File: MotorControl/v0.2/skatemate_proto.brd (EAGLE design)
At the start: 126.5 x 87.3 mm, 104 parts, among them IC1 REG1117, Q1 IRF740, Q2 IRF740, Q3 IRF740, Q4 IRF740, Q5 IRF740, Q6 IRF740, U1 DRV8301DCAR

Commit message: layouting on v0.2
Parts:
- removed Q1, Q2, Q3, Q4, Q5, Q6: IRF740, transistor-power:TO220BV
- removed SV1, SV2: (no value), skatemate:MA12-1
- added C39: 2u2, skatemate:C1206
- TP1: value TPSMD_M_1006 -> SUPPLY
- TP2: value TPSMD_M_1006 -> GND
- TP3: value TPSMD_M_1006 -> PH_A
- TP4: value TPSMD_M_1006 -> PH_B
- TP5: value TPSMD_M_1006 -> PH_C
- moved TP1 30.3 mm to (78.5, 7.62), turned to 90 degrees
- moved C6 28.0 mm to (83.8, 52.8), turned to 180 degrees
- moved C7 25.8 mm to (83.6, 30.0), turned to 180 degrees
- moved U$4 24.3 mm to (91.2, 71.4)
- moved U$6 24.3 mm to (91.2, 46.0)
- moved U$8 24.3 mm to (91.2, 20.6)
- moved U$5 17.1 mm to (98.8, 58.7), flipped to the bottom, turned to 90 degrees
- moved U$7 17.1 mm to (98.8, 33.3), flipped to the bottom, turned to 90 degrees
- moved U$9 17.1 mm to (98.8, 7.87), flipped to the bottom, turned to 90 degrees
- moved R6 15.8 mm to (87.6, 3.56), flipped to the bottom, turned to 180 degrees
- moved R4 15.7 mm to (92.7, 27.4), flipped to the bottom, turned to 180 degrees
- moved R2 15.7 mm to (92.7, 52.8), flipped to the bottom, turned to 180 degrees
- moved TP4 15.0 mm to (104.1, 46.0), flipped to the bottom, turned to 270 degrees
- moved TP5 14.8 mm to (104.1, 20.6), flipped to the bottom, turned to 270 degrees
- moved TP3 14.5 mm to (104.1, 71.4), flipped to the bottom, turned to 270 degrees
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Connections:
- net +5V: no longer SV1.3
- net ASENSE: no longer SV2.9
- net BSENSE: no longer SV2.10
- net CSENSE: no longer SV2.11
- net DRV_DCCAL: no longer SV1.11
- net DRV_EN_GATE: no longer SV1.12
- net DRV_NCS: no longer SV1.7
- net DRV_NFAULT: no longer SV1.6
- net DRV_NOCTW: no longer SV1.5
- net DRV_PWRGD: no longer SV1.4
- net DRV_SCK: no longer SV1.10
- net DRV_SDI: no longer SV1.8
- net DRV_SDO: no longer SV1.9
- net DRV_SOA: no longer SV2.7
- net DRV_SOB: no longer SV2.8
- net GND: now also C39.2; no longer Q6.S, SV1.2
- net INH_A: no longer SV2.1
- net INH_B: no longer SV2.3
- net INH_C: no longer SV2.5
- net INL_A: no longer SV2.2
- net INL_B: no longer SV2.4
- net INL_C: no longer SV2.6
- net N$10: no longer Q2.G
- net N$11: no longer Q3.G
- net N$12: no longer Q6.G
- net N$7: no longer Q1.G
- net N$8: no longer Q4.G
- net N$9: no longer Q5.G
- net PH_A: no longer Q1.S, Q4.D
- net PH_B: no longer Q2.S, Q5.D
- net PH_C: no longer Q3.S, Q6.D
- net SN_A: no longer Q4.S
- net SN_B: no longer Q5.S
- net SSENSE: no longer SV2.12
- net SUPPLY: now also C39.1; no longer Q1.D, Q2.D, Q3.D
- net VCC: no longer SV1.1
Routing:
- net VCC: track 317.3 -> 125.5 mm, vias 16 -> 7
- net SUPPLY: track 162.9 -> 18.9 mm, vias 3 -> 1
- net ASENSE: track 157.2 -> 37.8 mm, vias 2 -> 0
- net BSENSE: track 139.6 -> 41.6 mm, vias 2 -> 0
- net PH_B: track 93.3 -> 13.4 mm, vias 3 -> 1
- net PH_C: track 113.0 -> 35.8 mm, vias 3 -> 1
- net GND: track 267.1 -> 193.5 mm, vias 36 -> 30
- net CSENSE: track 122.8 -> 50.4 mm, vias 2 -> 0
- net PH_A: track 107.5 -> 42.0 mm, vias 3 -> 1
- net SN_A: track 95.8 -> 34.1 mm
- net SSENSE: track 115.1 -> 54.5 mm
- net SN_B: track 65.9 -> 14.2 mm, vias 2 -> 0
- net DRV_SCK: track 78.8 -> 45.0 mm
- net DRV_SDO: track 75.4 -> 42.8 mm
- net DRV_SDI: track 71.9 -> 39.9 mm
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- added copper zone on layer 16, net SN_A
- added copper zone on layer 16, net SN_B
- removed copper zone on layer 1, net +5V
- removed copper zone on layer 1, net SN_A
- removed copper zone on layer 1, net SN_B
- removed copper zone on layer 1, net SUPPLY
- removed copper zone on layer 1, net VCC
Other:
- board size 126.5 x 87.3 mm -> 167.4 x 87.6 mm
- board text added: "FHNW 2017 - p4 team 2"
- board text added: "skatemate-motorcontrol v0.2"
- board text removed: "FHNW 2017 - p2 team 2"
- board text removed: "skatemate-motorcontrol v0.1"

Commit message: Öpdeit, Meh gmoolet
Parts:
- moved U$3 45.6 mm to (62.5, 23.1), turned to 90 degrees
- moved R20 5.59 mm to (83.8, 9.65)
- moved C22 5.36 mm to (60.7, 64.8)
- moved D4 4.83 mm to (66.5, 63.8)
- moved R14 4.07 mm to (58.4, 64.0)
- moved R15 4.07 mm to (58.4, 68.1)
- moved L1 3.64 mm to (68.1, 70.6)
- moved C21 2.84 mm to (72.4, 33.3)
- moved D3 2.62 mm to (69.6, 5.33)
- moved D1 2.62 mm to (69.6, 12.4)
- moved D2 2.62 mm to (69.6, 8.89)
- moved D5 2.40 mm to (69.6, 1.78)
- moved R3 2.09 mm to (98.8, 51.3)
- moved C2 1.70 mm to (75.2, 37.6)
- moved C16 1.55 mm to (60.5, 37.8)
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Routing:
- net BSENSE: track 41.6 -> 139.3 mm, vias 0 -> 6
- net ASENSE: track 37.8 -> 134.8 mm, vias 0 -> 2
- net DRV_NCS: track 58.5 -> 17.1 mm, vias 1 -> 0
- net USB_D+: track 38.7 -> 0.00 mm, vias 4 -> 0
- net USB_D-: track 33.8 -> 1.25 mm, vias 4 -> 1
- net GND: track 193.5 -> 162.5 mm, vias 30 -> 29
- net VCC: track 125.5 -> 96.6 mm, vias 7 -> 1
- net GL_B: track 9.40 -> 35.6 mm, vias 0 -> 1
- net SN_A: track 34.1 -> 59.2 mm, vias 2 -> 4
- net DRV_SCK: track 45.0 -> 21.1 mm
- net DRV_SDO: track 42.8 -> 19.7 mm
- net DRV_SOB: track 48.1 -> 25.7 mm
- net DRV_SDI: track 39.9 -> 17.7 mm
- net DRV_SOA: track 47.1 -> 25.6 mm
- net CSENSE: track 50.4 -> 70.9 mm, vias 0 -> 4
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
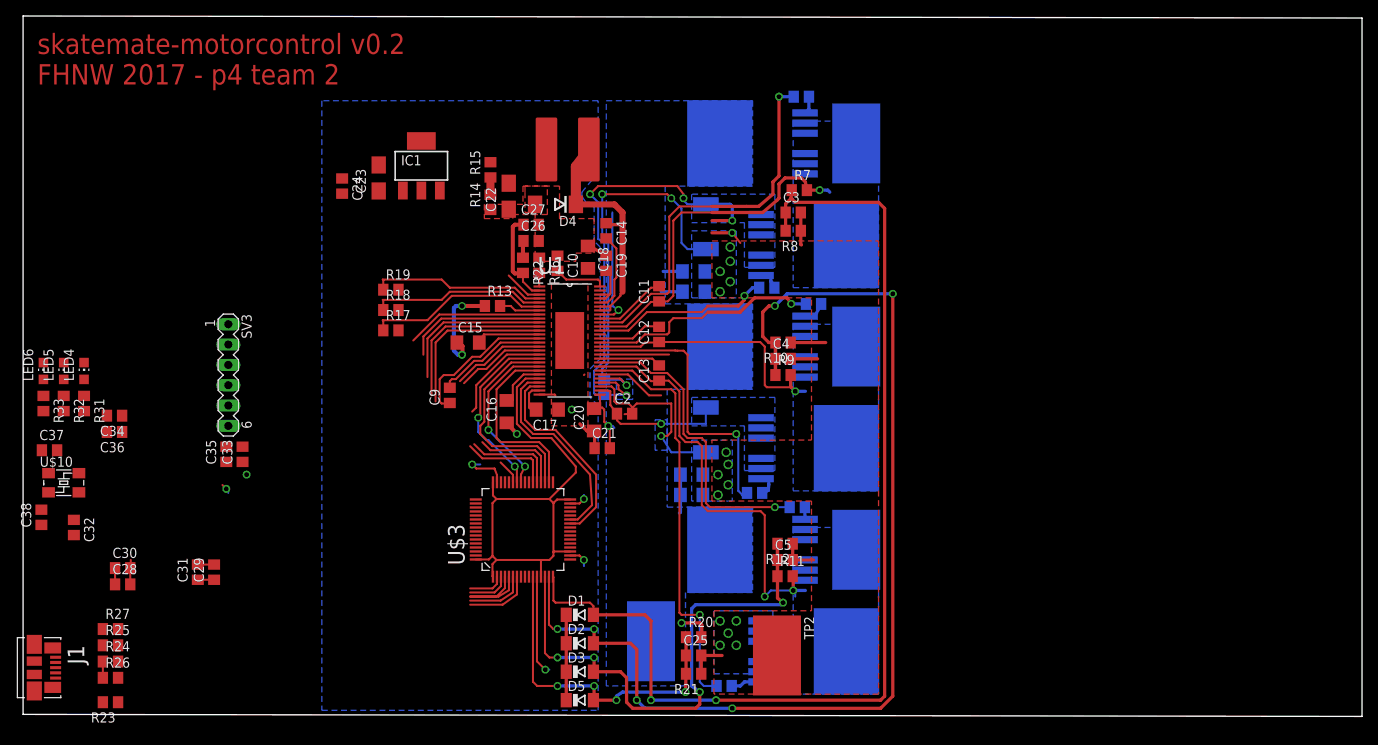
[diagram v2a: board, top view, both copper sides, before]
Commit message: no wiiter gmacht....
Kondensatoren noch unter IC pflanzen, Stecker Layouten, eine VCC Leitung
mit 100uF versehen.
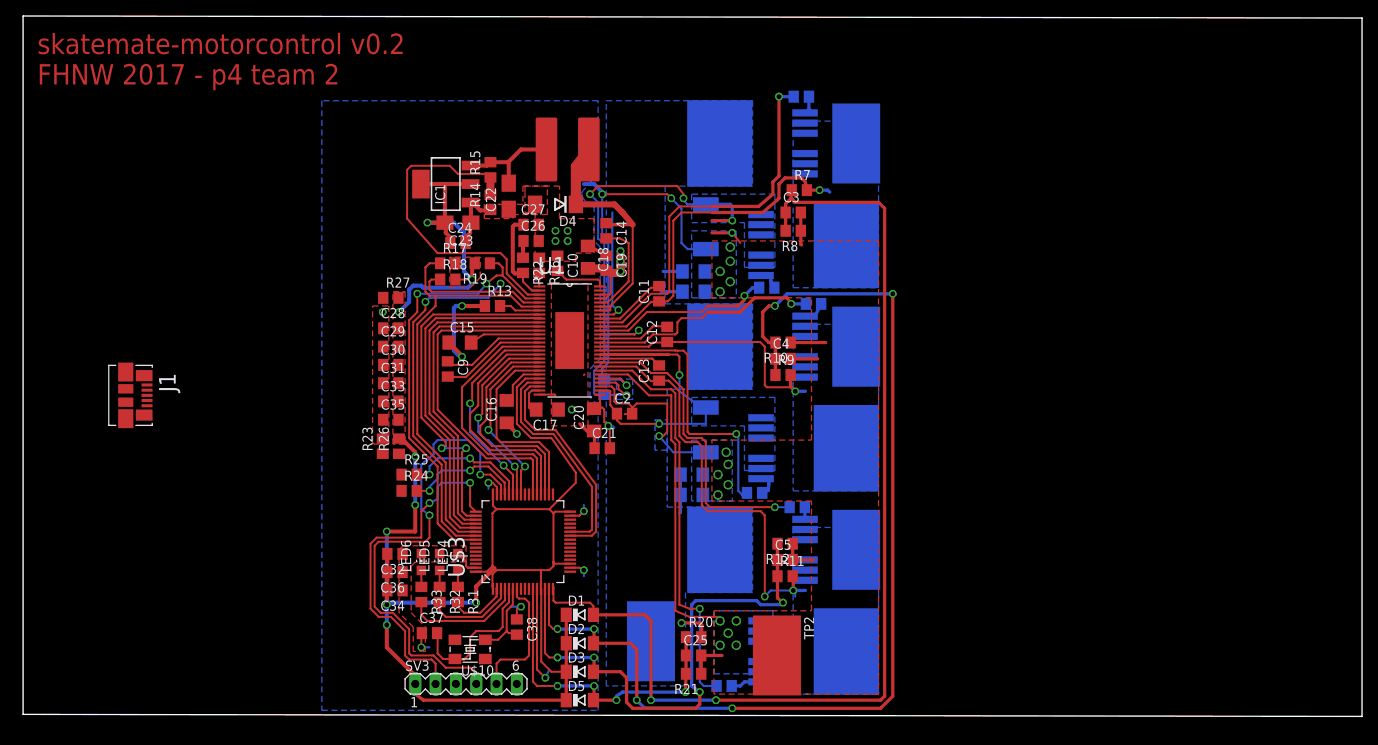
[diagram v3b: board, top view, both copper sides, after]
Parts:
- moved C38 61.0 mm to (61.7, 10.9), turned to 270 degrees
- moved U$10 54.9 mm to (55.9, 8.13), turned to 180 degrees
- moved R27 54.2 mm to (46.0, 52.1)
- moved LED6 52.9 mm to (49.8, 19.1)
- moved R33 52.9 mm to (49.8, 15.0)
- moved C37 52.7 mm to (50.8, 10.2)
- moved LED5 52.7 mm to (52.1, 19.1)
- moved R32 52.7 mm to (52.1, 15.0)
- moved LED4 52.5 mm to (54.4, 19.1)
- moved R31 52.5 mm to (54.4, 15.0)
- moved SV3 48.7 mm to (55.4, 3.81), turned to 0 degrees
- moved R23 46.7 mm to (45.0, 33.5), turned to 90 degrees
- moved C28 46.4 mm to (46.0, 48.3)
- moved R26 46.3 mm to (47.0, 33.5), turned to 90 degrees
- moved R24 43.0 mm to (48.3, 27.9)
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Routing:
- net VCC: track 96.6 -> 232.2 mm, vias 1 -> 10
- net SWDIO: track 0.00 -> 60.8 mm, vias 0 -> 2
- net GND: track 162.5 -> 210.9 mm, vias 29 -> 35
- net SWCLK: track 0.00 -> 46.2 mm, vias 0 -> 2
- net DRV_NOCTW: track 21.9 -> 62.8 mm, vias 0 -> 2
- net DRV_PWRGD: track 21.9 -> 56.4 mm, vias 0 -> 2
- net N$4: track 6.99 -> 41.3 mm
- net DRV_NFAULT: track 22.7 -> 54.9 mm
- net DRV_NCS: track 17.1 -> 45.3 mm, vias 0 -> 2
- net DRV_SDI: track 17.7 -> 43.7 mm
- net DRV_SDO: track 19.7 -> 41.7 mm
- net DRV_SCK: track 21.1 -> 40.0 mm
- net SN_B: track 27.2 -> 44.1 mm, vias 1 -> 2
- net USB_D+: track 0.00 -> 15.2 mm, vias 0 -> 2
- net USB_D-: track 1.25 -> 15.8 mm, vias 1 -> 2
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- added copper zone on layer 1, net VCC

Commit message: layout before review
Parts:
- moved J1 30.9 mm to (44.2, 28.4)
- moved C28 28.5 mm to (62.2, 24.9), flipped to the bottom, turned to 90 degrees
- moved C29 28.1 mm to (64.5, 24.9), flipped to the bottom, turned to 90 degrees
- moved C31 27.8 mm to (65.5, 21.6), flipped to the bottom, turned to 180 degrees
- moved C35 23.2 mm to (59.9, 18.3), flipped to the bottom, turned to 270 degrees
- moved C30 22.1 mm to (57.7, 24.9), flipped to the bottom, turned to 90 degrees
- moved R27 20.1 mm to (47.0, 32.0)
- moved C33 19.9 mm to (59.9, 24.9), flipped to the bottom, turned to 90 degrees
- moved C36 18.0 mm to (64.5, 18.3), flipped to the bottom, turned to 270 degrees
- moved C32 15.8 mm to (62.2, 18.3), flipped to the bottom, turned to 270 degrees
- moved C34 11.5 mm to (57.7, 18.3), flipped to the bottom, turned to 270 degrees
- moved R23 10.4 mm to (44.5, 23.1), turned to 180 degrees
- moved R26 7.64 mm to (47.5, 25.9), turned to 0 degrees
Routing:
- net VCC: track 232.2 -> 318.7 mm
- net SN_A: track 68.8 -> 84.9 mm, vias 5 -> 6
- net GND: track 210.9 -> 218.7 mm, vias 35 -> 42
- net N$22: track 0.00 -> 5.75 mm
- net N$23: track 0.00 -> 5.67 mm
- net SWDIO: track 60.8 -> 55.4 mm
- net SWCLK: track 46.2 -> 40.9 mm
- net N$25: track 0.00 -> 3.51 mm
- net N$24: track 0.00 -> 3.48 mm
- net SN_B: track 44.1 -> 45.6 mm
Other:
- board size 167.4 x 87.6 mm -> 72.1 x 81.7 mm

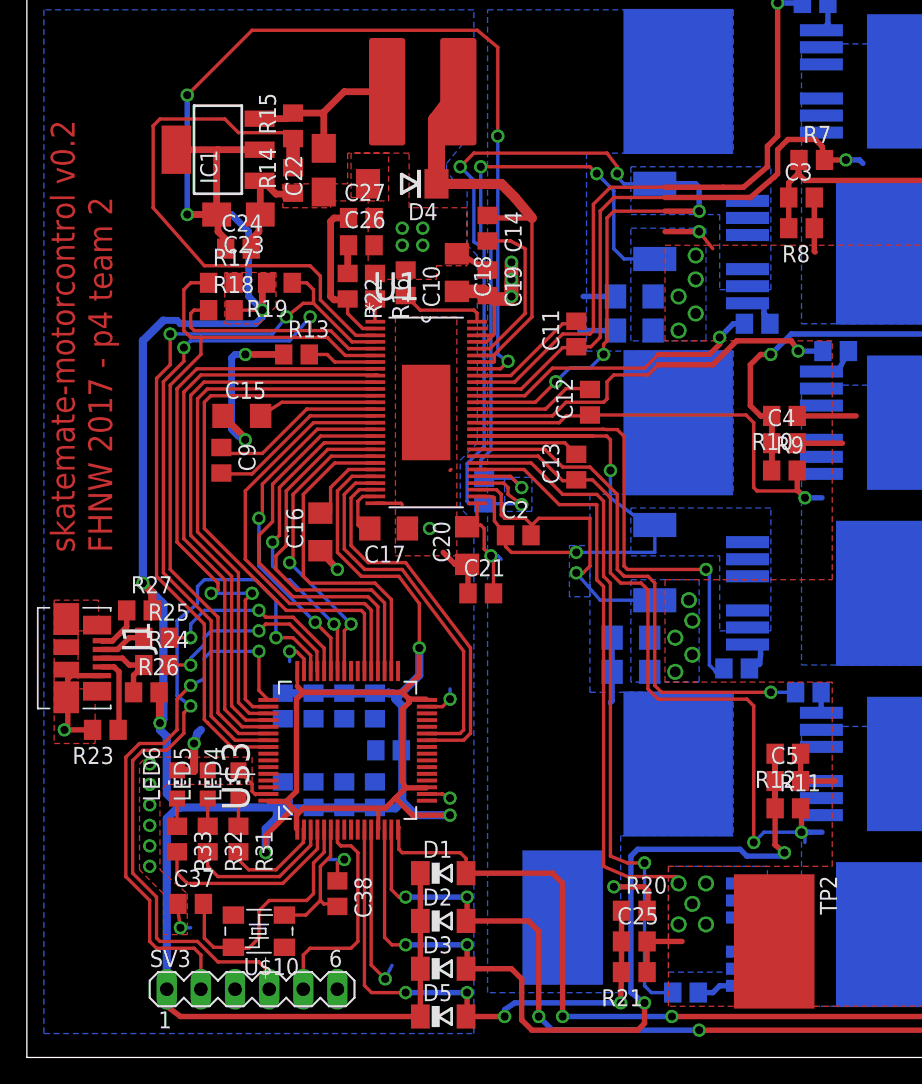
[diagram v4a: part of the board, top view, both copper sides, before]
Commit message: Parts renumber and BOM ULP
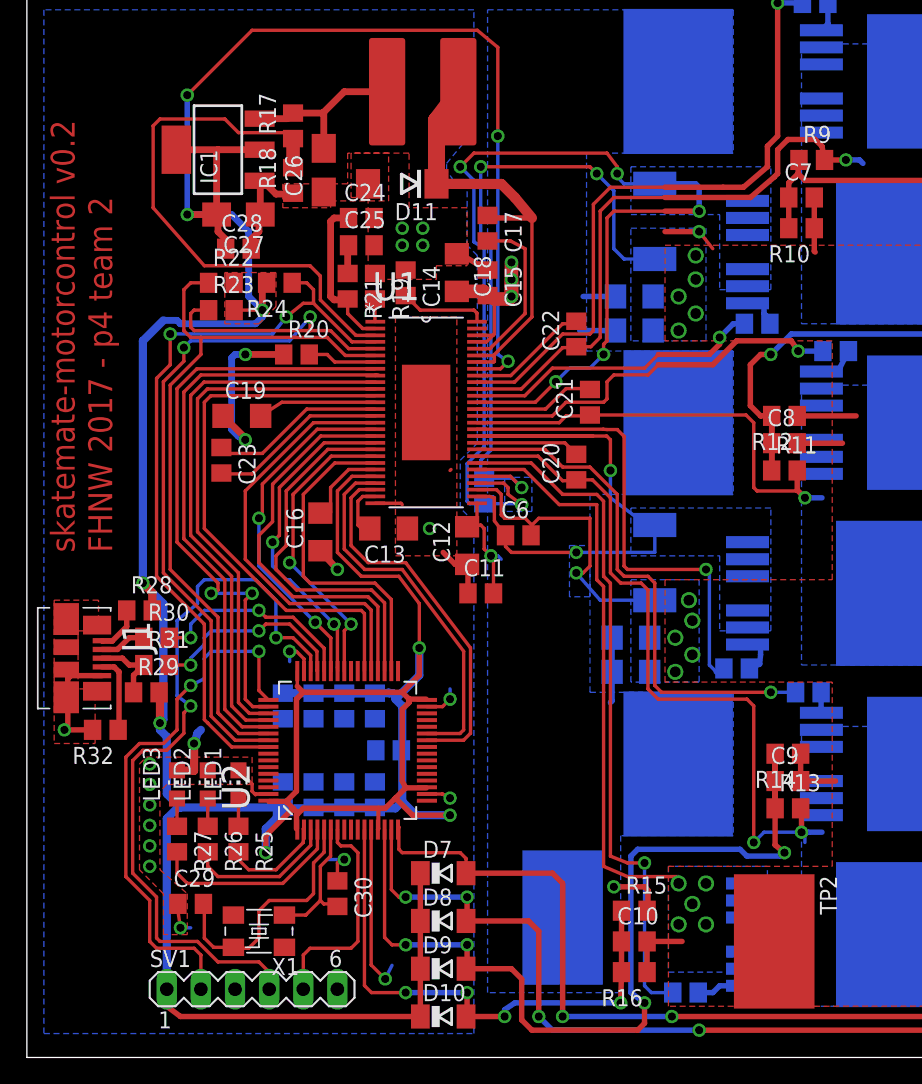
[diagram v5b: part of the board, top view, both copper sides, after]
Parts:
- removed R33: 3k3, skatemate:R0805
- removed U$1, U$2: R_EU, skatemate:R2512
- removed U$4, U$5, U$6, U$7, U$8: IRFS7534, skatemate:D2PAK-7
- added D10, D7, D8, D9: BAS85, skatemate:SOD80C
- added D11: SSA210, skatemate:DO-214AA
- added R28: 0 *, skatemate:R0805
- added R29: 1k5, skatemate:R0805
- added R30: 22, skatemate:R0805
- C10: value 10nF -> 47p
- C11, C21: value 0.1u -> 100n
- C12: value 0.1u -> 4u7; device skatemate:C0805 -> skatemate:C1206
- C13: value 0.1u -> 1u; device skatemate:C0805 -> skatemate:C1206
- C14: value 0.1u -> 10n
- C15: value 2.2u -> 100n; device skatemate:C1206 -> skatemate:C0805
- C17: value 1u -> 100n; device skatemate:C1206 -> skatemate:C0805
- C18: value 4.7u -> 4u7
- C19: value 0.1u -> 2u2; device skatemate:C0805 -> skatemate:C1206
- C2: value (none) -> 2u2; device skatemate:C0805 -> skatemate:C1206
- C20: value 4.7u -> 100n; device skatemate:C1206 -> skatemate:C0805
- C22: value 100u -> 100n; device skatemate:B/3528-21W -> skatemate:C0805
- C23: value 100u -> (none); device skatemate:B/3528-21W -> skatemate:C0805
- C24: value 0.1u -> 150p
- C25: value 47p -> 6n8
- C26: value 6n8 -> 100u; device skatemate:C0805 -> skatemate:B/3528-21W
- C27: value 150p -> 100u; device skatemate:C0805 -> skatemate:B/3528-21W
- C28, C33, C34: value 2u2 -> 100n
- C29: value 2u2 -> 22p
- C3, C4, C5: value 47p -> 2u2; device skatemate:C0805 -> skatemate:C1206
- C30: value 100n -> 22p
- C31, C32, C36: value 100n -> 2u2
- C37: value 22p -> 2u2
- C38: value 22p -> 100n
- C39: value 2u2 -> 100n; device skatemate:C1206 -> skatemate:C0805
- C6: value 2u2 -> (none); device skatemate:C1206 -> skatemate:C0805
- C7, C8: value 2u2 -> 47p; device skatemate:C1206 -> skatemate:C0805
- C9: value (none) -> 47p
- D1, D2, D3, D5: value BAS85 -> IRFS7534; device skatemate:SOD80C -> skatemate:D2PAK-7
- D4: value SSA210 -> IRFS7534; device skatemate:DO-214AA -> skatemate:D2PAK-7
- R13: value 10k -> 39k
- R14: value 3k3 -> 2k2
- R15: value 18k -> 39k
- R16: value 220k -> 2k2
- R18: value 18k -> 3k3
- R19: value 18k -> 220k
- R20: value 39k -> 10k
- R21: value 2k2 -> 16k
- R22: value 16k -> 18k
- R23: value 100k -> 18k
- R24: value 22 -> 18k
- R25: value 22 -> 3k3
- R26: value 1k5 -> 3k3
- R27: value 0 * -> 3k3
- R3, R6: value (none) -> R_EU; device skatemate:R0805 -> skatemate:R2512
- R31: value 3k3 -> 22
- R32: value 3k3 -> 100k
- R7: value 39k -> (none)
- R8: value 2k2 -> (none)
- moved R15 63.7 mm to (83.8, 9.65), turned to 0 degrees
- moved D1 62.8 mm to (91.2, 71.4), flipped to the bottom, turned to 270 degrees
- moved D2 57.7 mm to (98.8, 58.7), flipped to the bottom, turned to 90 degrees
- moved R8 57.5 mm to (87.6, 3.56), flipped to the bottom
- moved R14 56.4 mm to (95.2, 21.3), turned to 180 degrees
- moved C25 55.7 mm to (63.5, 59.2)
- moved R21 55.3 mm to (62.5, 56.1), turned to 270 degrees
- moved R16 54.6 mm to (83.8, 5.08), turned to 180 degrees
- moved C10 51.9 mm to (83.8, 7.37), turned to 0 degrees
- moved R13 49.8 mm to (95.2, 17.3)
- moved C9 48.5 mm to (95.2, 19.3), turned to 0 degrees
- moved R20 48.4 mm to (58.7, 51.1)
- moved D3 46.0 mm to (91.2, 46.0), flipped to the bottom, turned to 270 degrees
- moved D4 44.4 mm to (98.8, 33.3), flipped to the bottom, turned to 90 degrees
- moved C39 41.8 mm to (64.5, 18.3), turned to 270 degrees
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- renumbered LED4 to LED1, LED5 to LED2, LED6 to LED3, SV3 to SV1, U$10 to X1, U$3 to U2, U$9 to D6
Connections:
- net +5V: now also C26.+, R17.2; no longer C22.+, R15.2
- net ASENSE: now also C7.1, D7.A, R10.2, R9.1; no longer C3.1, D1.A, R7.1, R8.2
- net BSENSE: now also C8.1, D8.A, R11.1, R12.2; no longer C4.1, D2.A, R10.2, R9.1
- net BST_BK: now also C17.1, D11.C; no longer C14.1, D4.C
- net CSENSE: now also C9.1, D9.A, R13.1, R14.2; no longer C5.1, D3.A, R11.1, R12.2
- net DRV_NFAULT: now also R22.1; no longer R17.1
- net DRV_NOCTW: now also R23.1; no longer R18.1
- net DRV_PWRGD: now also R24.1; no longer R19.1
- net GH_B: now also R4.1; no longer R3.1
- net GH_C: now also R7.1; no longer R5.1
- net GL_B: now also R5.1; no longer R4.1
- net GL_C: now also R8.1; no longer R6.1
- net GND: now also C10.2, C11.1, C12.1, C13.1, C14.1, C26.-, C27.-, C28.2, C39.1, C9.2, D11.A, R18.1, R19.1, R20.1, R3.2, R32.2, R6.2; no longer C10.1, C17.1, C20.1, C21.1, C22.-, C23.-, C26.2, C27.2, C28.1, C39.2, D4.A, R13.1, R21.1, R23.2, R8.1, U$1.2, U$2.2
- net N$1: now also C23.2; no longer C9.2
- net N$10: now also D3.G, R4.2; no longer R3.2, U$6.G
- net N$11: now also D5.G, R7.2; no longer R5.2, U$8.G
- net N$12: now also R8.2; no longer R6.2
- net N$13: now also C22.2; no longer C11.2
- net N$14: now also C21.2; no longer C12.2
- net N$15: now also C20.2; no longer C13.2
- net N$16: now also C17.2; no longer C14.2
- net N$17: now also C19.2; no longer C15.2
- net N$19: now also C13.2; no longer C17.2
- net N$2: now also C23.1; no longer C9.1
- net N$20: now also C24.1, R21.2; no longer C27.1, R22.2
- net N$21: now also C25.1, R21.1; no longer C26.1, R22.1
- net N$22: now also R32.1; no longer R23.1
- net N$23: now also R29.1, R31.1; no longer R24.1, R26.1
- net N$24: now also R30.1; no longer R25.1
- net N$25: now also R28.1; no longer R27.1
- net N$28: now also R27.2; no longer R33.2
- net N$29: now also R26.2; no longer R32.2
- net N$3: now also R20.2; no longer R13.2
- net N$30: now also R25.2; no longer R31.2
- net N$31: now also R25.1; no longer R31.1
- net N$32: now also R26.1; no longer R32.1
- net N$33: now also R27.1; no longer R33.1
- net N$35: now also C30.2; no longer C38.2
- net N$36: now also C29.2; no longer C37.2
- net N$4: now also R17.1, R18.2; no longer R14.2, R15.1
- net N$5: now also C14.2; no longer C10.2
- net N$6: now also R19.2; no longer R16.2
- net N$7: now also D1.G; no longer U$4.G
- net N$8: now also D2.G; no longer U$5.G
- net N$9: now also D4.G, R5.2; no longer R4.2, U$7.G
- net PH_A: now also C22.1, D1.S1, D1.S2, D1.S3, D1.S4, D1.S5, D2.D, R9.2; no longer C11.1, R7.2, U$4.S1, U$4.S2, U$4.S3, U$4.S4, U$4.S5, U$5.D
- net PH_B: now also C21.1, D3.S1, D3.S2, D3.S3, D3.S4, D3.S5, D4.D, R11.2; no longer C12.1, R9.2, U$6.S1, U$6.S2, U$6.S3, U$6.S4, U$6.S5, U$7.D
- net PH_C: now also C20.1, D5.S1, D5.S2, D5.S3, D5.S4, D5.S5, R13.2; no longer C13.1, R11.2, U$8.S1, U$8.S2, U$8.S3, U$8.S4, U$8.S5
- net SN_A: now also D2.S1, D2.S2, D2.S3, D2.S4, D2.S5, R3.1; no longer U$1.1, U$5.S1, U$5.S2, U$5.S3, U$5.S4, U$5.S5
- net SN_B: now also C6.1, D4.S1, D4.S2, D4.S3, D4.S4, D4.S5, R6.1; no longer C2.1, U$2.1, U$7.S1, U$7.S2, U$7.S3, U$7.S4, U$7.S5
- net SSENSE: now also C10.1, D10.A, R15.1, R16.2; no longer C25.1, D5.A, R20.1, R21.2
- net SUPPLY: now also C11.2, C12.2, C15.2, C2.1, C3.1, C4.1, C5.1, D1.D, D3.D, D5.D, R15.2; no longer C19.2, C20.2, C21.2, C39.1, C6.1, C7.1, C8.1, R20.2, U$4.D, U$6.D, U$8.D
- net USB_D+: now also R31.2; no longer R24.2
- net USB_D-: now also R30.2; no longer R25.2
- net VCC: now also C27.+, C28.1, C37.2, C38.2, C39.2, D10.C, D7.C, D8.C, D9.C, R22.2, R23.2, R24.2, R28.2, R29.2; no longer C23.+, C24.1, C28.2, C29.2, C30.2, D1.C, D2.C, D3.C, D5.C, R17.2, R18.2, R19.2, R26.2, R27.2
